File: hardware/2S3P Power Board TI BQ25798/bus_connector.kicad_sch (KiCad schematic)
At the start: 1 part, among them J401 53426-1210

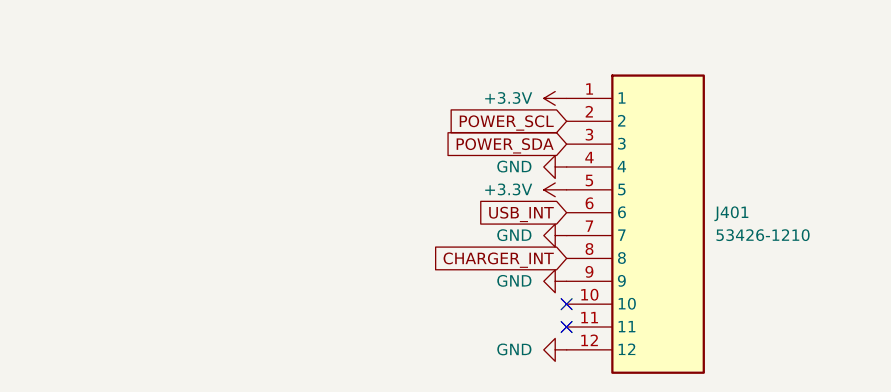
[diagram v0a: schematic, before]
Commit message: Switch to Molex 12 circuit Pico-Lock header, part# 504050-1291
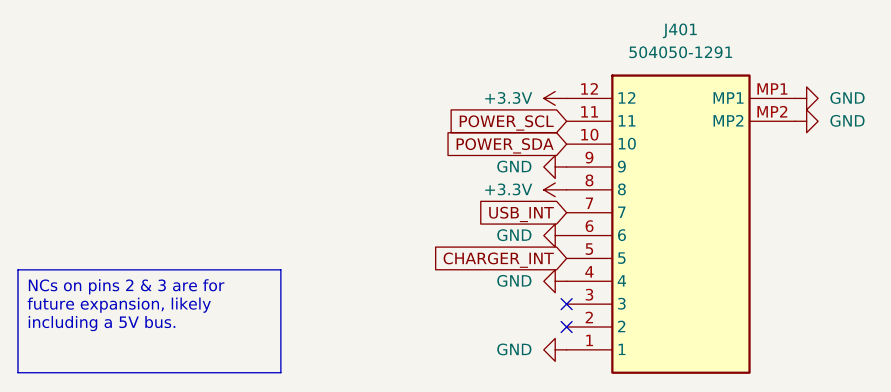
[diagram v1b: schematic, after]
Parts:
- removed J401: 53426-1210, footprints:534261210, symbol Molex 53426-1210:53426-1210
- added J401: 504050-1291, footprints:5040501291, symbol Molex 504050-1291:504050-1291
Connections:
- net +3.3V: now also J401.12, J401.8
- net CHARGER_INT: now also J401.5
- net GND: now also J401.1, J401.4, J401.6, J401.9, J401.MP1, J401.MP2
- net POWER_SCL: now also J401.11
- net POWER_SDA: now also J401.10
- net USB_INT: now also J401.7
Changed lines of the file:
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@@
   (no_connect (at 132.08 106.68))
   (no_connect (at 132.08 104.14))
+  (text_box "NCs on pins 2 & 3 are for future expansion, likely including a 5V bus."
+    (at 71.12 100.33 0) (size 29.21 11.43)
+    (stroke (width 0) (type default))
+    (fill (type none))
+    (effects (font (size 1.27 1.27)) (justify left top))
+  )
   (global_label "USB_INT" (shape input) (at 132.08 93.98 180) (fields_autoplaced)
     (effects (font (size 1.27 1.27)) (justify right))
@@
     )
   )
-  (symbol (lib_id "Molex 53426-1210:53426-1210") (at 132.08 81.28 0) (unit 1)
+  (symbol (lib_id "Molex 504050-1291:504050-1291") (at 132.08 81.28 0) (unit 1)
     (in_bom yes) (on_board yes) (dnp no) (fields_autoplaced)
-    (property "Reference" "J401" (at 148.59 93.98 0)
-      (effects (font (size 1.27 1.27)) (justify left))
+    (property "Reference" "J401" (at 144.78 73.66 0)
+      (effects (font (size 1.27 1.27)))
     )
-    (property "Value" "53426-1210" (at 148.59 96.52 0)
-      (effects (font (size 1.27 1.27)) (justify left))
+    (property "Value" "504050-1291" (at 144.78 76.2 0)
+      (effects (font (size 1.27 1.27)))
     )
-    (property "Footprint" "footprints:534261210" (at 148.59 176.2 0)
+    (property "Footprint" "footprints:5040501291" (at 153.67 176.2 0)
       (effects (font (size 1.27 1.27)) (justify left top) hide)
     )
-    (property "Datasheet" "https://www.mouser.com/datasheet/2/276/0534261410_PCB_HEADERS-693578.pdf" (at 148.59 276.2 0)
+    (property "Datasheet" "" (at 153.67 276.2 0)
       (effects (font (size 1.27 1.27)) (justify left top) hide)
     )
-    (property "Height" "6.7" (at 148.59 476.2 0)
+    (property "Height" "2.15" (at 153.67 476.2 0)
       (effects (font (size 1.27 1.27)) (justify left top) hide)
     )
-    (property "Manufacturer_Name" "Molex" (at 148.59 576.2 0)
+    (property "Manufacturer_Name" "Molex" (at 153.67 576.2 0)
       (effects (font (size 1.27 1.27)) (justify left top) hide)
     )
-    (property "Manufacturer_Part_Number" "53426-1210" (at 148.59 676.2 0)
+    (property "Manufacturer_Part_Number" "504050-1291" (at 153.67 676.2 0)
       (effects (font (size 1.27 1.27)) (justify left top) hide)
     )
-    (property "Mouser Part Number" "538-53426-1210" (at 148.59 776.2 0)
+    (property "Mouser Part Number" "538-504050-1291" (at 153.67 776.2 0)
       (effects (font (size 1.27 1.27)) (justify left top) hide)
     )
-    (property "Mouser Price/Stock" "https://www.mouser.co.uk/ProductDetail/Molex/53426-1210?qs=naUSJSqnqcJ6jsGMjYRA3g%3D%3D" (at 148.59 876.2 0)
+    (property "Mouser Price/Stock" "https://www.mouser.co.uk/ProductDetail/Molex/504050-1291?qs=IvkZ4pJZlB2rki3iIhyJgg%3D%3D" (at 153.67 876.2 0)
       (effects (font (size 1.27 1.27)) (justify left top) hide)
     )
-    (property "Arrow Part Number" "" (at 148.59 976.2 0)
+    (property "Arrow Part Number" "" (at 153.67 976.2 0)
       (effects (font (size 1.27 1.27)) (justify left top) hide)
     )
-    (property "Arrow Price/Stock" "" (at 148.59 1076.2 0)
+    (property "Arrow Price/Stock" "" (at 153.67 1076.2 0)
       (effects (font (size 1.27 1.27)) (justify left top) hide)
     )
+    (property "MPN" "C563982" (at 132.08 81.28 0)
+      (effects (font (size 1.27 1.27)) hide)
+    )
+    (property "Manufacturer" "MOLEX" (at 132.08 81.28 0)
+      (effects (font (size 1.27 1.27)) hide)
+    )
+    (property "Manufacturer Part Number" "504050-1291" (at 132.08 81.28 0)
+      (effects (font (size 1.27 1.27)) hide)
+    )
+    (pin "MP2")
+    (pin "10")
+    (pin "1")
+    (pin "6")
+    (pin "7")
+    (pin "8")
+    (pin "4")
+    (pin "9")
     (pin "5")
-    (pin "4")
-    (pin "6")
-    (pin "1")
-    (pin "8")
+    (pin "2")
+    (pin "11")
+    (pin "MP1")
     (pin "3")
-    (pin "10")
     (pin "12")
-    (pin "11")
-    (pin "9")
-    (pin "2")
-    (pin "7")
     (instances
       (project "2S3P Power Board TI BQ25798"
@@
         )
       )
+    )
+  )
+  (symbol (lib_id "power:GND") (at 157.48 81.28 90) (unit 1)
+    (in_bom yes) (on_board yes) (dnp no) (fields_autoplaced)
+    (property "Reference" "#PWR0407" (at 163.83 81.28 0)
+      (effects (font (size 1.27 1.27)) hide)
+    )
+    (property "Value" "GND" (at 161.29 81.28 90)
+      (effects (font (size 1.27 1.27)) (justify right))
+    )
+    (property "Footprint" "" (at 157.48 81.28 0)
+      (effects (font (size 1.27 1.27)) hide)
+    )
+    (property "Datasheet" "" (at 157.48 81.28 0)
+      (effects (font (size 1.27 1.27)) hide)
+    )
+    (pin "1")
+    (instances
+      (project "2S3P Power Board TI BQ25798"
+        (path "/d7fbba2e-84c5-4e09-9d36-52dae726d12d/f5dda946-81da-4978-88f4-4ac2bc2b63d0"
+          (reference "#PWR0407") (unit 1)
+        )
+      )
+    )
+  )
+  (symbol (lib_id "power:GND") (at 157.48 83.82 90) (unit 1)
+    (in_bom yes) (on_board yes) (dnp no) (fields_autoplaced)
+    (property "Reference" "#PWR0408" (at 163.83 83.82 0)
+      (effects (font (size 1.27 1.27)) hide)
+    )
+    (property "Value" "GND" (at 161.29 83.82 90)
+      (effects (font (size 1.27 1.27)) (justify right))
+    )
+    (property "Footprint" "" (at 157.48 83.82 0)
+      (effects (font (size 1.27 1.27)) hide)
+    )
+    (property "Datasheet" "" (at 157.48 83.82 0)
+      (effects (font (size 1.27 1.27)) hide)
+    )
+    (pin "1")
+    (instances
+      (project "2S3P Power Board TI BQ25798"
+        (path "/d7fbba2e-84c5-4e09-9d36-52dae726d12d/f5dda946-81da-4978-88f4-4ac2bc2b63d0"
+          (reference "#PWR0408") (unit 1)
+        )
+      )

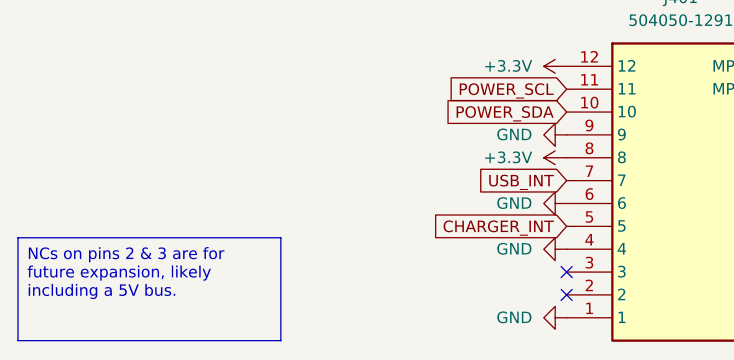
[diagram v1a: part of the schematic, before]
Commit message: Added test points and extra text explanations
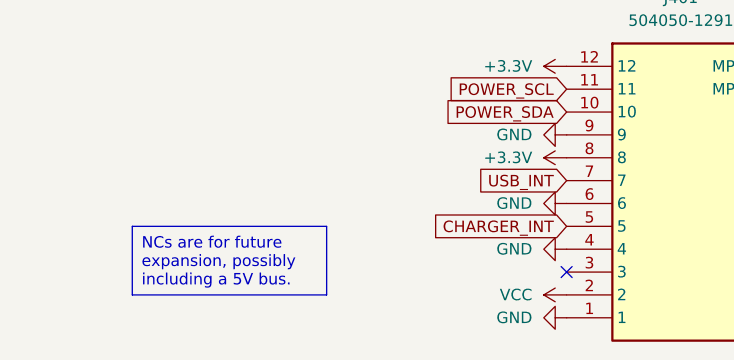
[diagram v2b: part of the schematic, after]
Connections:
- net VCC: now reaches J401.2
- no-connect marks 2 -> 1
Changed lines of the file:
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@@
 (kicad_sch (version 20230121) (generator eeschema)
   (paper "USLetter")
-  (no_connect (at 132.08 106.68))
   (no_connect (at 132.08 104.14))
-  (text_box "NCs on pins 2 & 3 are for future expansion, likely including a 5V bus."
-    (at 71.12 100.33 0) (size 29.21 11.43)
+  (text_box "NCs are for future expansion, possibly including a 5V bus."
+    (at 83.82 99.06 0) (size 21.59 7.62)
     (stroke (width 0) (type default))
     (fill (type none))
@@
         )
       )
+    )
+  )
+  (symbol (lib_id "power:VCC") (at 132.08 106.68 90) (unit 1)
+    (in_bom yes) (on_board yes) (dnp no) (fields_autoplaced)
+    (property "Reference" "#PWR0409" (at 135.89 106.68 0)
+      (effects (font (size 1.27 1.27)) hide)
+    )
+    (property "Value" "VCC" (at 128.27 106.68 90)
+      (effects (font (size 1.27 1.27)) (justify left))
+    )
+    (property "Footprint" "" (at 132.08 106.68 0)
+      (effects (font (size 1.27 1.27)) hide)
+    )
+    (property "Datasheet" "" (at 132.08 106.68 0)
+      (effects (font (size 1.27 1.27)) hide)
+    )
+    (pin "1")
+    (instances
+      (project "2S3P Power Board TI BQ25798"
+        (path "/d7fbba2e-84c5-4e09-9d36-52dae726d12d/f5dda946-81da-4978-88f4-4ac2bc2b63d0"
+          (reference "#PWR0409") (unit 1)
+        )
+      )

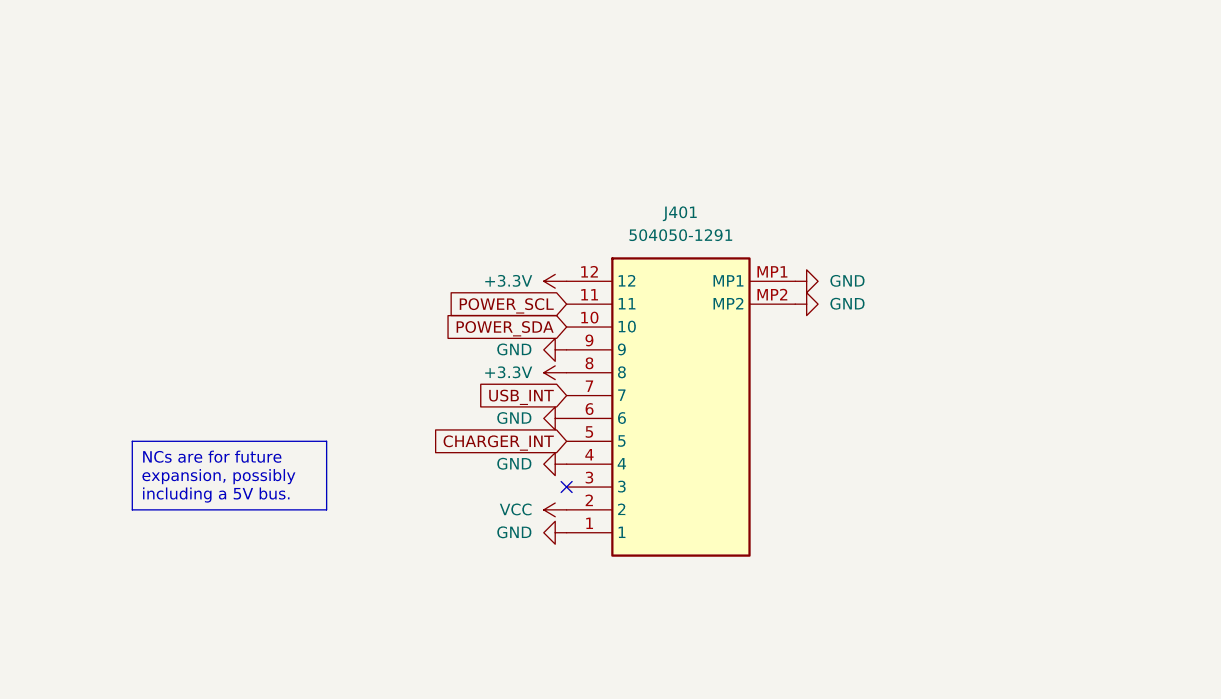
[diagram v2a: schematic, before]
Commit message: Swapped out USB connector for one from Amphenol that has better availability.
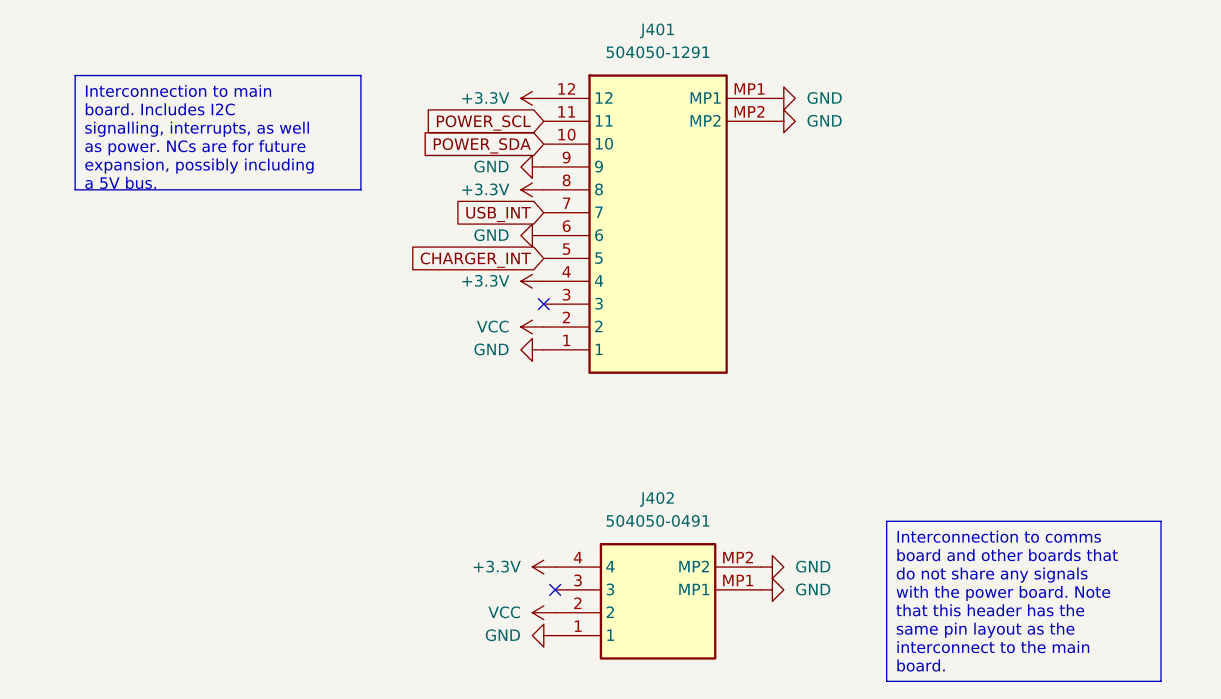
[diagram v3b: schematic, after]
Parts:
- added J402: 504050-0491, footprints:5040500491, symbol Molex 504050-0491:504050-0491
- J401: Active (none) -> Y
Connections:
- net +3.3V: now also J401.4, J402.4
- net GND: now also J402.1, J402.MP1, J402.MP2; no longer J401.4
- net VCC: now also J402.2
- no-connect marks 1 -> 2
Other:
- moved on the sheet: J401

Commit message: Modified USB control to use the BQ25798 directly
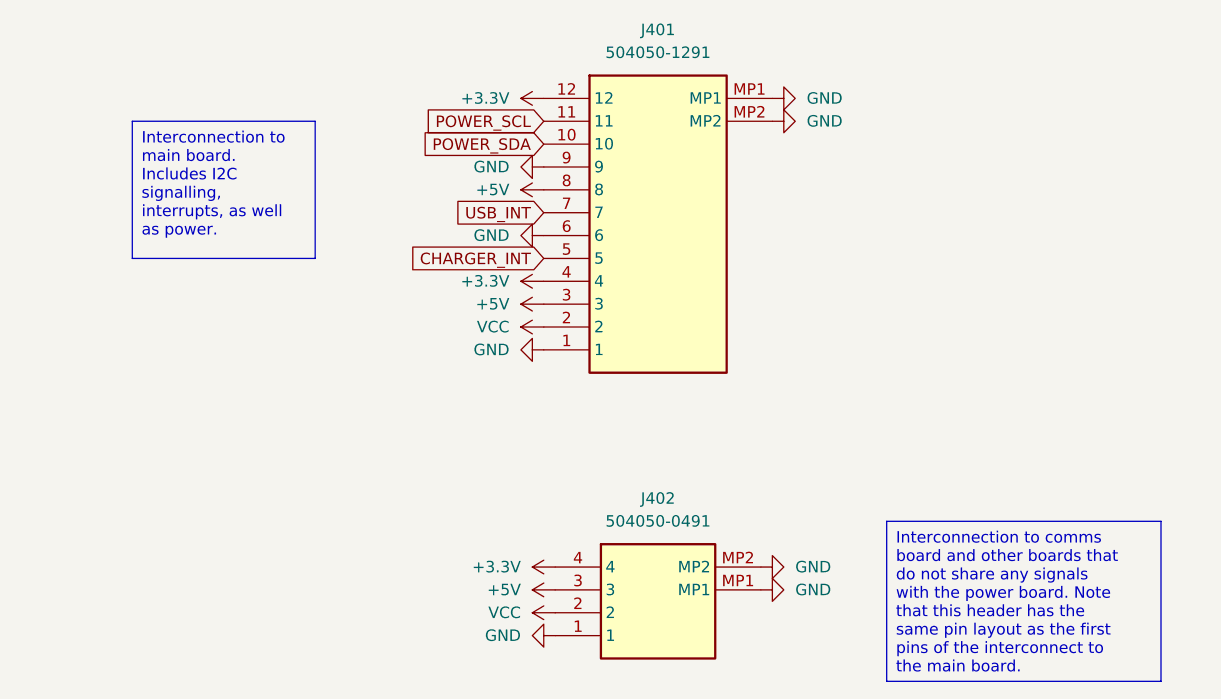
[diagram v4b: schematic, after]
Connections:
- net +3.3V: no longer J401.8
- net +5V: now reaches J401.3
- net +5V: now also J401.8, J402.3
- no-connect marks 2 -> 0
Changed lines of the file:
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@@
 (kicad_sch (version 20230121) (generator eeschema)
   (paper "USLetter")
-  (no_connect (at 129.54 83.82))
-  (no_connect (at 130.81 115.57))
-  (text_box "Interconnection to main board. Includes I2C signalling, interrupts, as well as power. NCs are for future expansion, possibly including a 5V bus."
-    (at 77.47 58.42 0) (size 31.75 12.7)
+  (text_box "Interconnection to main board. Includes I2C signalling, interrupts, as well as power."
+    (at 83.82 63.5 0) (size 20.32 15.24)
     (stroke (width 0) (type default))
     (fill (type none))
     (effects (font (size 1.27 1.27)) (justify left top))
   )
-  (text_box "Interconnection to comms board and other boards that do not share any signals with the power board. Note that this header has the same pin layout as the interconnect to the main board."
+  (text_box "Interconnection to comms board and other boards that do not share any signals with the power board. Note that this header has the same pin layout as the first pins of the interconnect to the main board."
     (at 167.64 107.95 0) (size 30.48 17.78)
     (stroke (width 0) (type default))
@@
     )
   )
+  (symbol (lib_id "power:+5V") (at 129.54 83.82 90) (unit 1)
+    (in_bom yes) (on_board yes) (dnp no) (fields_autoplaced)
+    (property "Reference" "#PWR0416" (at 133.35 83.82 0)
+      (effects (font (size 1.27 1.27)) hide)
+    )
+    (property "Value" "+5V" (at 125.73 83.82 90)
+      (effects (font (size 1.27 1.27)) (justify left))
+    )
+    (property "Footprint" "" (at 129.54 83.82 0)
+      (effects (font (size 1.27 1.27)) hide)
+    )
+    (property "Datasheet" "" (at 129.54 83.82 0)
+      (effects (font (size 1.27 1.27)) hide)
+    )
+    (pin "1")
+    (instances
+      (project "2S3P Power Board TI BQ25798"
+        (path "/d7fbba2e-84c5-4e09-9d36-52dae726d12d/f5dda946-81da-4978-88f4-4ac2bc2b63d0"
+          (reference "#PWR0416") (unit 1)
+        )
+      )
+    )
+  )
   (symbol (lib_id "power:VCC") (at 130.81 118.11 90) (unit 1)
     (in_bom yes) (on_board yes) (dnp no) (fields_autoplaced)
@@
     )
   )
+  (symbol (lib_id "power:+5V") (at 130.81 115.57 90) (unit 1)
+    (in_bom yes) (on_board yes) (dnp no) (fields_autoplaced)
+    (property "Reference" "#PWR0415" (at 134.62 115.57 0)
+      (effects (font (size 1.27 1.27)) hide)
+    )
+    (property "Value" "+5V" (at 127 115.57 90)
+      (effects (font (size 1.27 1.27)) (justify left))
+    )
+    (property "Footprint" "" (at 130.81 115.57 0)
+      (effects (font (size 1.27 1.27)) hide)
+    )
+    (property "Datasheet" "" (at 130.81 115.57 0)
+      (effects (font (size 1.27 1.27)) hide)
+    )
+    (pin "1")
+    (instances
+      (project "2S3P Power Board TI BQ25798"
+        (path "/d7fbba2e-84c5-4e09-9d36-52dae726d12d/f5dda946-81da-4978-88f4-4ac2bc2b63d0"
+          (reference "#PWR0415") (unit 1)
+        )
+      )
+    )
+  )
+  (symbol (lib_id "power:+5V") (at 129.54 71.12 90) (unit 1)
+    (in_bom yes) (on_board yes) (dnp no) (fields_autoplaced)
+    (property "Reference" "#PWR0404" (at 133.35 71.12 0)
+      (effects (font (size 1.27 1.27)) hide)
+    )
+    (property "Value" "+5V" (at 125.73 71.12 90)
+      (effects (font (size 1.27 1.27)) (justify left))
+    )
+    (property "Footprint" "" (at 129.54 71.12 0)
+      (effects (font (size 1.27 1.27)) hide)
+    )
+    (property "Datasheet" "" (at 129.54 71.12 0)
+      (effects (font (size 1.27 1.27)) hide)
+    )
+    (pin "1")
+    (instances
+      (project "2S3P Power Board TI BQ25798"
+        (path "/d7fbba2e-84c5-4e09-9d36-52dae726d12d/f5dda946-81da-4978-88f4-4ac2bc2b63d0"
+          (reference "#PWR0404") (unit 1)
+        )
+      )
+    )
+  )
   (symbol (lib_id "power:GND") (at 130.81 120.65 270) (unit 1)
     (in_bom yes) (on_board yes) (dnp no) (fields_autoplaced)
@@
         )
       )
-    )
-  )
-  (symbol (lib_id "power:+3.3V") (at 129.54 71.12 90) (unit 1)
-    (in_bom yes) (on_board yes) (dnp no) (fields_autoplaced)
-    (property "Reference" "#PWR0404" (at 133.35 71.12 0)
-      (effects (font (size 1.27 1.27)) hide)
-    )
-    (property "Value" "+3.3V" (at 125.73 71.12 90)
-      (effects (font (size 1.27 1.27)) (justify left))
-    )
-    (property "Footprint" "" (at 129.54 71.12 0)
-      (effects (font (size 1.27 1.27)) hide)
-    )
-    (property "Datasheet" "" (at 129.54 71.12 0)
-      (effects (font (size 1.27 1.27)) hide)
-    )
-    (pin "1")
-    (instances
-      (project "2S3P Power Board TI BQ25798"
-        (path "/d7fbba2e-84c5-4e09-9d36-52dae726d12d/f5dda946-81da-4978-88f4-4ac2bc2b63d0"
-          (reference "#PWR0404") (unit 1)
-        )
-      )

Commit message: Reordered the sheets
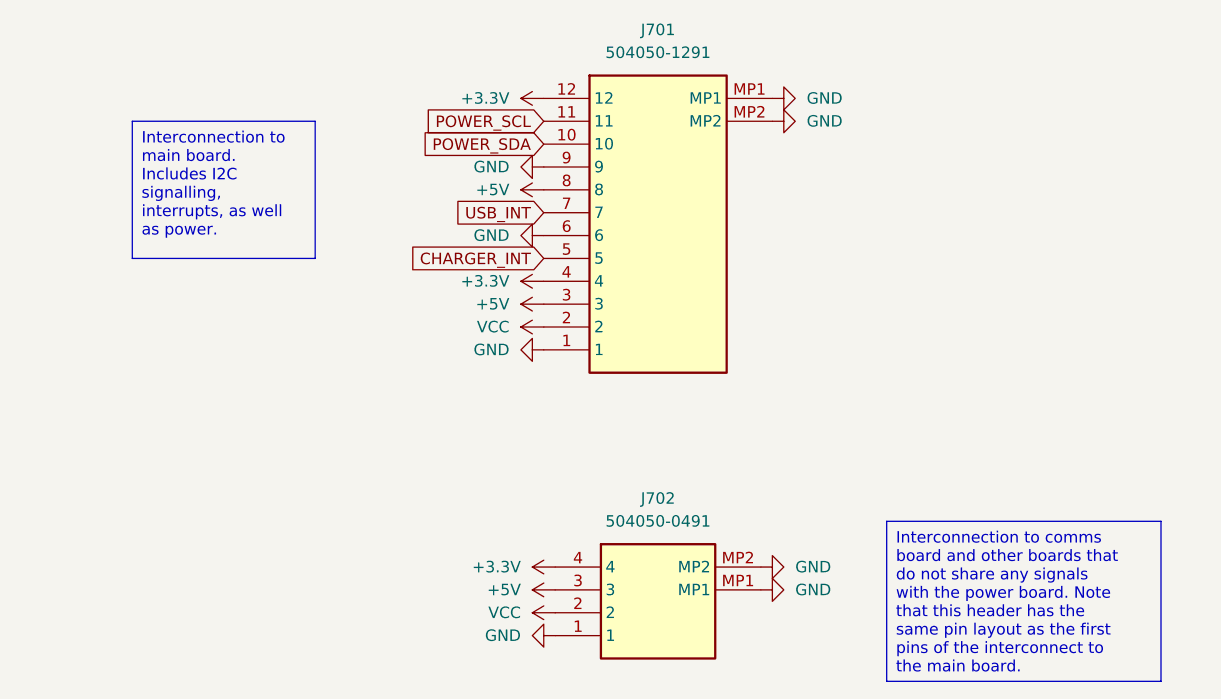
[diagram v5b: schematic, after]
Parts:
- renumbered J401 to J701, J402 to J702

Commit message: Fixed JLCPCB part number on a connector
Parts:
- J702: MPN C587992 -> C177235
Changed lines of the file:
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@@
       (effects (font (size 1.27 1.27)) hide)
     )
-    (property "MPN" "C587992" (at 130.81 113.03 0)
+    (property "MPN" "C177235" (at 130.81 113.03 0)
       (effects (font (size 1.27 1.27)) hide)
     )

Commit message: Checkpointing work after feedback from team
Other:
- note added: "Still used?"
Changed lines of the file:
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@@
     (effects (font (size 1.27 1.27)) (justify left top))
+  )
+  (text "Still used?\n" (at 109.22 74.93 0)
+    (effects (font (size 1.27 1.27)) (justify left bottom))
   )
   (global_label "USB_INT" (shape input) (at 129.54 73.66 180) (fields_autoplaced)
